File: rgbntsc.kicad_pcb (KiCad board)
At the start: 2 copper layers, 50 x 70 mm, 40 parts, among them J1 USB_C_Receptacle_Power, J2 VGA, J3 SCART_CONN, J4 Mini-DIN-4, U1 LM1881, U102 74AHCT1G86, U103 74AHCT1G86, U2 SC6206B-65K5, U3 CXA2075, X1 ASE-14.32MHz

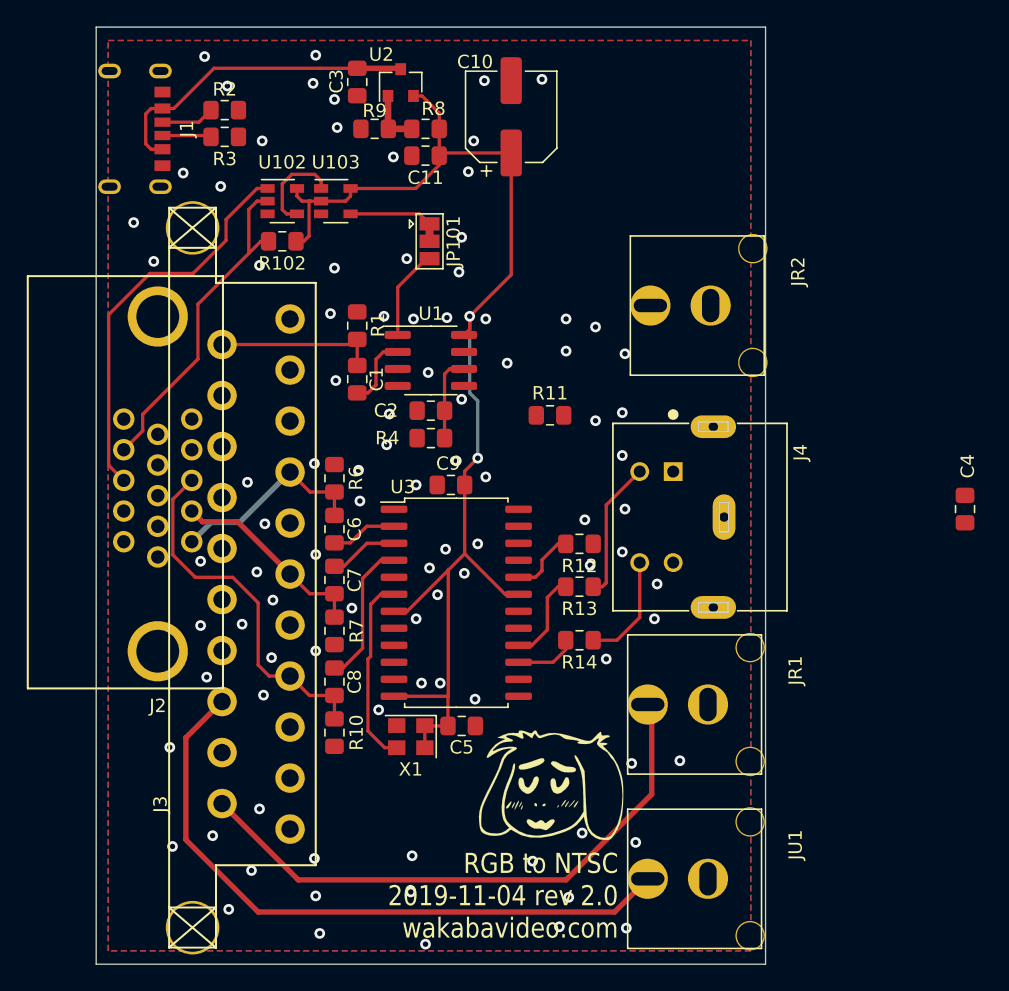
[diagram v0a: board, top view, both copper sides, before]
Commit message: added 1v amp and output caps
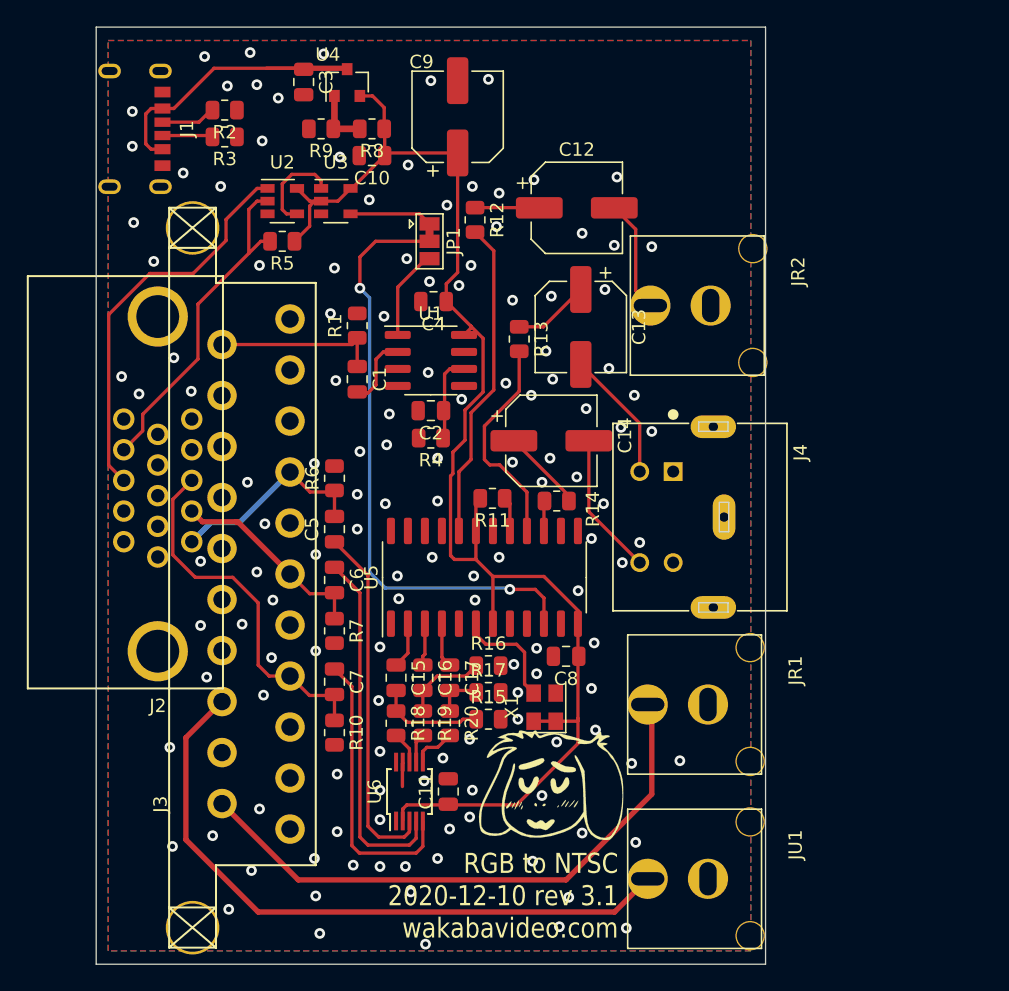
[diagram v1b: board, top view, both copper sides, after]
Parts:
- removed the C11 at (44.6, 49.6)
- removed the U2 at (42.7, 44.1)
- added C12: 220u, Capacitor_SMD:CP_Elec_6.3x5.4, F.Cu at (55.9, 53.5)
- added C13: 220u, Capacitor_SMD:CP_Elec_6.3x5.4, F.Cu at (56.2, 62.4)
- added C14: 220u, Capacitor_SMD:CP_Elec_6.3x5.4, F.Cu at (54.0, 70.9)
- added C15: 1u, Capacitor_SMD:C_0805_2012Metric, F.Cu at (42.4, 88.6)
- added C16: 1u, Capacitor_SMD:C_0805_2012Metric, F.Cu at (44.4, 88.6)
- added C17: 1u, Capacitor_SMD:C_0805_2012Metric, F.Cu at (46.4, 88.6)
- added C9: 33u, Capacitor_SMD:CP_Elec_6.3x7.7, F.Cu at (47.0, 46.7)
- added R15: 180, Resistor_SMD:R_0805_2012Metric, F.Cu at (49.3, 91.7)
- added R16: 180, Resistor_SMD:R_0805_2012Metric, F.Cu at (49.3, 87.7)
- added R17: 180, Resistor_SMD:R_0805_2012Metric, F.Cu at (49.3, 89.7)
- added R18: 75, Resistor_SMD:R_0805_2012Metric, F.Cu at (42.4, 92.0)
- added R19: 75, Resistor_SMD:R_0805_2012Metric, F.Cu at (44.4, 92.0)
- added R20: 75, Resistor_SMD:R_0805_2012Metric, F.Cu at (46.4, 92.0)
- added U4: SC6206B-65K5, Package_TO_SOT_SMD:SOT-23, F.Cu at (38.7, 44.1)
- added U6: TPF144-VR, Package_SO:MSOP-10_3x3mm_P0.5mm, F.Cu at (43.4, 97.1)
- C1, C2, C3, C4: footprint Capacitor_SMD:C_0805_2012Metric_Pad1.15x1.40mm_HandSolder -> Capacitor_SMD:C_0805_2012Metric
- C10: value 33u -> 10u; footprint Capacitor_SMD:CP_Elec_6.3x7.7 -> Capacitor_SMD:C_0805_2012Metric
- C11: renamed from C5; footprint Capacitor_SMD:C_0805_2012Metric_Pad1.15x1.40mm_HandSolder -> Capacitor_SMD:C_0805_2012Metric
- C5: renamed from C6; footprint Capacitor_SMD:C_0805_2012Metric_Pad1.15x1.40mm_HandSolder -> Capacitor_SMD:C_0805_2012Metric
- C6: renamed from C7; footprint Capacitor_SMD:C_0805_2012Metric_Pad1.15x1.40mm_HandSolder -> Capacitor_SMD:C_0805_2012Metric
- C7: renamed from C8; footprint Capacitor_SMD:C_0805_2012Metric_Pad1.15x1.40mm_HandSolder -> Capacitor_SMD:C_0805_2012Metric
- C8: renamed from C9; footprint Capacitor_SMD:C_0805_2012Metric_Pad1.15x1.40mm_HandSolder -> Capacitor_SMD:C_0805_2012Metric
- R1, R10, R11, R12, R13, R14, R2, R3, R4, R6, R7: footprint Resistor_SMD:R_0805_2012Metric_Pad1.15x1.40mm_HandSolder -> Resistor_SMD:R_0805_2012Metric
- R5: renamed from R102; footprint Resistor_SMD:R_0805_2012Metric_Pad1.15x1.40mm_HandSolder -> Resistor_SMD:R_0805_2012Metric
- R8: value 3k -> 1k; footprint Resistor_SMD:R_0805_2012Metric_Pad1.15x1.40mm_HandSolder -> Resistor_SMD:R_0805_2012Metric
- R9: value 1k -> 1k3; footprint Resistor_SMD:R_0805_2012Metric_Pad1.15x1.40mm_HandSolder -> Resistor_SMD:R_0805_2012Metric
- U5: renamed from U3; footprint Package_SO:SOP-24_7.5x15.4mm_P1.27mm -> Package_SO:SO-24_5.3x15mm_P1.27mm
- X1: value ASE-14.32MHz -> O32253579545MHEA4SI
- moved C4 42.6 mm to (45.2, 60.5), turned to 180 degrees
- moved R12 25.4 mm to (48.3, 54.4), turned to 270 degrees
- moved R13 19.0 mm to (51.6, 63.3), turned to 270 degrees
- moved C8 15.4 mm to (55.1, 87.0)
- moved C10 10.8 mm to (40.6, 49.6), turned to 180 degrees
- moved R14 10.5 mm to (54.4, 75.4)
- moved X1 10.2 mm to (53.5, 90.8), turned to 90 degrees
- moved R11 7.55 mm to (49.6, 75.2), turned to 180 degrees
- moved C11 5.00 mm to (46.3, 97.1), turned to 90 degrees
- moved C3 4.00 mm to (35.5, 44.1)
- moved R8 4.00 mm to (40.6, 47.6)
- moved R9 4.00 mm to (36.8, 47.6)
- moved U5 2.83 mm to (49.0, 81.1), turned to 90 degrees
- renumbered JP101 to JP1, U102 to U2, U103 to U3
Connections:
- C5 pad 1: Net-(C6-Pad1) -> Net-(C5-Pad1)
- C6 pad 1: Net-(C7-Pad1) -> Net-(C6-Pad1)
- C7 pad 1: Net-(C8-Pad1) -> Net-(C7-Pad1)
- J4 pad 3: Net-(J4-Pad3) -> Net-(C13-Pad2)
- J4 pad 4: Net-(J4-Pad4) -> Net-(C14-Pad2)
- JR2 pad 1: Net-(JR2-Pad1) -> Net-(C12-Pad2)
- R12 pad 1: Net-(JR2-Pad1) -> Net-(C12-Pad1)
- R13 pad 1: Net-(J4-Pad3) -> Net-(C13-Pad1)
- R14 pad 1: Net-(J4-Pad4) -> Net-(C14-Pad1)
- U5 pad 10: Net-(U3-Pad10) -> /SYNC
- U5 pad 2: Net-(C6-Pad1) -> Net-(C15-Pad1)
- U5 pad 3: Net-(C7-Pad1) -> Net-(C16-Pad1)
- U5 pad 4: Net-(C8-Pad1) -> Net-(C17-Pad1)
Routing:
- net /SYNC: track 0.00 -> 45.3 mm, vias 0 -> 2
- net Net-(C5-Pad1): track 0.00 -> 26.7 mm
- net Net-(C6-Pad1): track 4.96 -> 26.9 mm
- net Net-(R12-Pad2): track 5.03 -> 24.0 mm
- net Net-(C7-Pad1): track 5.16 -> 21.4 mm
- net VCC: track 93.2 -> 105.9 mm, vias 2 -> 0
- net Net-(C8-Pad1): track 10.8 -> 0.00 mm
- net Net-(C14-Pad2): track 0.00 -> 10.7 mm
- net Net-(J4-Pad3): track 10.4 -> 0.00 mm
- net Net-(C13-Pad2): track 0.00 -> 9.82 mm
- net Net-(R13-Pad2): track 6.76 -> 16.2 mm
- net Net-(C12-Pad2): track 0.00 -> 8.42 mm
- net Net-(J4-Pad4): track 8.28 -> 0.00 mm
- net Net-(C15-Pad2): track 0.00 -> 7.97 mm
- net Net-(C16-Pad2): track 0.00 -> 6.29 mm
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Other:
- board text added: "RGB to NTSC 2020-12-10 rev 3.1 wakabavideo.com"
- board text removed: "RGB to NTSC 2019-11-04 rev 2.0 wakabavideo.com"
